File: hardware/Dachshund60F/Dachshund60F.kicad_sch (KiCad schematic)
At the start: 0 parts

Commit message: Add Dachshund60F schematic and PCB placement
- Schematic (one A2 sheet, 195 parts, ERC clean): MDBT50Q-1MV2 with
  32.768 kHz crystal, SWD and reset; MCP73831 charger (500 mA), JST-PH
  battery and power switch into VDDH; TPS22917-switched SK6812MINI-E
  LEDs; EC11 encoder; 6x15 COL2ROW matrix with 80 positions; JST-SH
  connector for a USB-C daughterboard. Module pins match board.json.
- PCB: all footprints placed from the KLE layout. Switches, stabilizers
  and encoder on the front, every SMD part on the back, and an 18 mm
  top strip for the module (antenna at the edge) and power parts.
  Not routed yet.
- Kailh MX hot-swap everywhere except SW604, SW606 and SW615, which use
  solder-only 3-pin footprints so the 6.25u and split spacebars can
  overlap.
- Vendor the keyswitch footprints (perigoso v2.4, CC-BY-SA-4.0) into
  hardware/Dachshund60F/lib, upgraded to the KiCad 10 format so Konnect
  can read them.
- .mcp.json: pin KiCad's IPC socket for Konnect.
- PROGRESS.md and the board README: design decisions and known DRC
  findings.

Co-Authored-By: Claude Opus 5.5 <noreply@anthropic.com>
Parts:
- added C1, C2, C3, C4, C6: 4.7uF, Capacitor_SMD:C_0603_1608Metric, symbol Device:C
- added C10, C11: 10nF, Capacitor_SMD:C_0402_1005Metric, symbol Device:C
- added C12: 1uF, Capacitor_SMD:C_0402_1005Metric, symbol Device:C
- added C13, C14, C5, C7: 100nF, Capacitor_SMD:C_0402_1005Metric, symbol Device:C
- added C8, C9: 12pF, Capacitor_SMD:C_0402_1005Metric, symbol Device:C
- added D1: BAT54WS, Diode_SMD:D_SOD-323, symbol Device:D_Schottky
- added D100, D101, D102, D103, D104, D105, D106, D107, D108, D109, D110, D111, D112, D113, D114, D200, D201, D202, D203, D204, D205, D206, D207, D208, D209, D210, D211, D212, D213, D300, D301, D302, D303, D304, D305, D306, D307, D308, D309, D310, D311, D312, D313, D400, D401, D402, D403, D404, D405, D406, D407, D408, D409, D410, D411, D413, D500, D501, D502, D503, D504, D505, D506, D507, D508, D509, D510, D512, D513, D600, D601, D603, D604, D606, D608, D610, D611, D612, D613, D614: 1N4148W, Diode_SMD:D_SOD-123, symbol Device:D
- added D2: SK6812MINI-E (Caps), LED_SMD:LED_SK6812MINI-E_3.2x2.8mm_P1.5mm_ReverseMount, symbol LED:SK6812MINI-E
- added D3: SK6812MINI-E (Layer), LED_SMD:LED_SK6812MINI-E_3.2x2.8mm_P1.5mm_ReverseMount, symbol LED:SK6812MINI-E
- added J1: USB daughterboard (JST-SH 4P), Connector_JST:JST_SH_SM04B-SRSS-TB_1x04-1MP_P1.00mm_Horizontal, symbol Connector_Generic_MountingPin:Conn_01x04_MountingPin
- added J2: Battery (JST-PH 2P), Connector_JST:JST_PH_S2B-PH-SM4-TB_1x02-1MP_P2.00mm_Horizontal, symbol Connector_Generic_MountingPin:Conn_01x02_MountingPin
- added J3: SWD, Connector_PinHeader_1.27mm:PinHeader_1x05_P1.27mm_Vertical, symbol Connector_Generic:Conn_01x05
- added R1: 2k, Resistor_SMD:R_0603_1608Metric, symbol Device:R
- added R2: 100k, Resistor_SMD:R_0402_1005Metric, symbol Device:R
- added ST1: Stab Backspace 2.00u, Keyswitch:Stabilizer_Cherry_MX_2.00u, symbol Mechanical:MountingHole
- added ST2: Stab Enter 2.25u, Keyswitch:Stabilizer_Cherry_MX_2.00u, symbol Mechanical:MountingHole
- added ST3: Stab Shift 2.25u, Keyswitch:Stabilizer_Cherry_MX_2.00u, symbol Mechanical:MountingHole
- added ST4: Stab Space 6.25u, Keyswitch:Stabilizer_Cherry_MX_6.25u, symbol Mechanical:MountingHole
- added ST5: Stab Space 2.75u, Keyswitch:Stabilizer_Cherry_MX_2.00u, symbol Mechanical:MountingHole
- added ST6: Stab Mod 2.25u, Keyswitch:Stabilizer_Cherry_MX_2.00u, symbol Mechanical:MountingHole
- added SW1: Power, Button_Switch_SMD:SW_SPDT_PCM12, symbol Switch:SW_SPDT
- added SW100: MX Esc (1.00u), Keyswitch:SW_Hotswap_Kailh_MX_1.00u, symbol Switch:SW_Push
- added SW101: MX F1 (1.00u), Keyswitch:SW_Hotswap_Kailh_MX_1.00u, symbol Switch:SW_Push
- added SW102: MX F2 (1.00u), Keyswitch:SW_Hotswap_Kailh_MX_1.00u, symbol Switch:SW_Push
- added SW103: MX F3 (1.00u), Keyswitch:SW_Hotswap_Kailh_MX_1.00u, symbol Switch:SW_Push
- added SW104: MX F4 (1.00u), Keyswitch:SW_Hotswap_Kailh_MX_1.00u, symbol Switch:SW_Push
- added SW105: MX F5 (1.00u), Keyswitch:SW_Hotswap_Kailh_MX_1.00u, symbol Switch:SW_Push
- added SW106: MX F6 (1.00u), Keyswitch:SW_Hotswap_Kailh_MX_1.00u, symbol Switch:SW_Push
- added SW107: MX F7 (1.00u), Keyswitch:SW_Hotswap_Kailh_MX_1.00u, symbol Switch:SW_Push
- added SW108: MX F8 (1.00u), Keyswitch:SW_Hotswap_Kailh_MX_1.00u, symbol Switch:SW_Push
- added SW109: MX F9 (1.00u), Keyswitch:SW_Hotswap_Kailh_MX_1.00u, symbol Switch:SW_Push
- added SW110: MX F10 (1.00u), Keyswitch:SW_Hotswap_Kailh_MX_1.00u, symbol Switch:SW_Push
- added SW111: MX F11 (1.00u), Keyswitch:SW_Hotswap_Kailh_MX_1.00u, symbol Switch:SW_Push
- added SW112: MX F12 (1.00u), Keyswitch:SW_Hotswap_Kailh_MX_1.00u, symbol Switch:SW_Push
- added SW113: MX Delete (1.00u), Keyswitch:SW_Hotswap_Kailh_MX_1.00u, symbol Switch:SW_Push
- added SW2: Reset, Button_Switch_SMD:SW_SPST_TL3342, symbol Switch:SW_Push
- added SW200: MX ` (1.00u), Keyswitch:SW_Hotswap_Kailh_MX_1.00u, symbol Switch:SW_Push
- added SW201: MX 1 (1.00u), Keyswitch:SW_Hotswap_Kailh_MX_1.00u, symbol Switch:SW_Push
- added SW202: MX 2 (1.00u), Keyswitch:SW_Hotswap_Kailh_MX_1.00u, symbol Switch:SW_Push
- added SW203: MX 3 (1.00u), Keyswitch:SW_Hotswap_Kailh_MX_1.00u, symbol Switch:SW_Push
- added SW204: MX 4 (1.00u), Keyswitch:SW_Hotswap_Kailh_MX_1.00u, symbol Switch:SW_Push
- added SW205: MX 5 (1.00u), Keyswitch:SW_Hotswap_Kailh_MX_1.00u, symbol Switch:SW_Push
- added SW206: MX 6 (1.00u), Keyswitch:SW_Hotswap_Kailh_MX_1.00u, symbol Switch:SW_Push
- added SW207: MX 7 (1.00u), Keyswitch:SW_Hotswap_Kailh_MX_1.00u, symbol Switch:SW_Push
- added SW208: MX 8 (1.00u), Keyswitch:SW_Hotswap_Kailh_MX_1.00u, symbol Switch:SW_Push
- added SW209: MX 9 (1.00u), Keyswitch:SW_Hotswap_Kailh_MX_1.00u, symbol Switch:SW_Push
- added SW210: MX 0 (1.00u), Keyswitch:SW_Hotswap_Kailh_MX_1.00u, symbol Switch:SW_Push
- added SW211: MX - (1.00u), Keyswitch:SW_Hotswap_Kailh_MX_1.00u, symbol Switch:SW_Push
- added SW212: MX = (1.00u), Keyswitch:SW_Hotswap_Kailh_MX_1.00u, symbol Switch:SW_Push
- added SW213: MX Backspace (2.00u), Keyswitch:SW_Hotswap_Kailh_MX_2.00u, symbol Switch:SW_Push
- added SW3: EC11E encoder, Rotary_Encoder:RotaryEncoder_Alps_EC11E-Switch_Vertical_H20mm, symbol Device:RotaryEncoder_Switch_MP
- added SW300: MX Tab (1.50u), Keyswitch:SW_Hotswap_Kailh_MX_1.50u, symbol Switch:SW_Push
- added SW301: MX Q (1.00u), Keyswitch:SW_Hotswap_Kailh_MX_1.00u, symbol Switch:SW_Push
- added SW302: MX W (1.00u), Keyswitch:SW_Hotswap_Kailh_MX_1.00u, symbol Switch:SW_Push
- added SW303: MX E (1.00u), Keyswitch:SW_Hotswap_Kailh_MX_1.00u, symbol Switch:SW_Push
- added SW304: MX R (1.00u), Keyswitch:SW_Hotswap_Kailh_MX_1.00u, symbol Switch:SW_Push
- added SW305: MX T (1.00u), Keyswitch:SW_Hotswap_Kailh_MX_1.00u, symbol Switch:SW_Push
- added SW306: MX Y (1.00u), Keyswitch:SW_Hotswap_Kailh_MX_1.00u, symbol Switch:SW_Push
- added SW307: MX U (1.00u), Keyswitch:SW_Hotswap_Kailh_MX_1.00u, symbol Switch:SW_Push
- added SW308: MX I (1.00u), Keyswitch:SW_Hotswap_Kailh_MX_1.00u, symbol Switch:SW_Push
- added SW309: MX O (1.00u), Keyswitch:SW_Hotswap_Kailh_MX_1.00u, symbol Switch:SW_Push
- added SW310: MX P (1.00u), Keyswitch:SW_Hotswap_Kailh_MX_1.00u, symbol Switch:SW_Push
- added SW311: MX [ (1.00u), Keyswitch:SW_Hotswap_Kailh_MX_1.00u, symbol Switch:SW_Push
- added SW312: MX ] (1.00u), Keyswitch:SW_Hotswap_Kailh_MX_1.00u, symbol Switch:SW_Push
- added SW313: MX \ (1.50u), Keyswitch:SW_Hotswap_Kailh_MX_1.50u, symbol Switch:SW_Push
- added SW400: MX Caps Lock (1.75u), Keyswitch:SW_Hotswap_Kailh_MX_1.75u, symbol Switch:SW_Push
- added SW401: MX A (1.00u), Keyswitch:SW_Hotswap_Kailh_MX_1.00u, symbol Switch:SW_Push
- added SW402: MX S (1.00u), Keyswitch:SW_Hotswap_Kailh_MX_1.00u, symbol Switch:SW_Push
- added SW403: MX D (1.00u), Keyswitch:SW_Hotswap_Kailh_MX_1.00u, symbol Switch:SW_Push
- added SW404: MX F (1.00u), Keyswitch:SW_Hotswap_Kailh_MX_1.00u, symbol Switch:SW_Push
- added SW405: MX G (1.00u), Keyswitch:SW_Hotswap_Kailh_MX_1.00u, symbol Switch:SW_Push
- added SW406: MX H (1.00u), Keyswitch:SW_Hotswap_Kailh_MX_1.00u, symbol Switch:SW_Push
- added SW407: MX J (1.00u), Keyswitch:SW_Hotswap_Kailh_MX_1.00u, symbol Switch:SW_Push
- added SW408: MX K (1.00u), Keyswitch:SW_Hotswap_Kailh_MX_1.00u, symbol Switch:SW_Push
- added SW409: MX L (1.00u), Keyswitch:SW_Hotswap_Kailh_MX_1.00u, symbol Switch:SW_Push
- added SW410: MX ; (1.00u), Keyswitch:SW_Hotswap_Kailh_MX_1.00u, symbol Switch:SW_Push
- added SW411: MX ' (1.00u), Keyswitch:SW_Hotswap_Kailh_MX_1.00u, symbol Switch:SW_Push
- added SW413: MX Enter (2.25u), Keyswitch:SW_Hotswap_Kailh_MX_2.25u, symbol Switch:SW_Push
- added SW500: MX Shift (2.25u), Keyswitch:SW_Hotswap_Kailh_MX_2.25u, symbol Switch:SW_Push
- added SW501: MX Z (1.00u), Keyswitch:SW_Hotswap_Kailh_MX_1.00u, symbol Switch:SW_Push
- added SW502: MX X (1.00u), Keyswitch:SW_Hotswap_Kailh_MX_1.00u, symbol Switch:SW_Push
- added SW503: MX C (1.00u), Keyswitch:SW_Hotswap_Kailh_MX_1.00u, symbol Switch:SW_Push
- added SW504: MX V (1.00u), Keyswitch:SW_Hotswap_Kailh_MX_1.00u, symbol Switch:SW_Push
- added SW505: MX B (1.00u), Keyswitch:SW_Hotswap_Kailh_MX_1.00u, symbol Switch:SW_Push
- added SW506: MX N (1.00u), Keyswitch:SW_Hotswap_Kailh_MX_1.00u, symbol Switch:SW_Push
- added SW507: MX M (1.00u), Keyswitch:SW_Hotswap_Kailh_MX_1.00u, symbol Switch:SW_Push
- added SW508: MX , (1.00u), Keyswitch:SW_Hotswap_Kailh_MX_1.00u, symbol Switch:SW_Push
- added SW509: MX . (1.00u), Keyswitch:SW_Hotswap_Kailh_MX_1.00u, symbol Switch:SW_Push
- added SW510: MX / (1.00u), Keyswitch:SW_Hotswap_Kailh_MX_1.00u, symbol Switch:SW_Push
- added SW512: MX Shift (1.75u), Keyswitch:SW_Hotswap_Kailh_MX_1.75u, symbol Switch:SW_Push
- added SW513: MX Up (1.00u), Keyswitch:SW_Hotswap_Kailh_MX_1.00u, symbol Switch:SW_Push
- added SW600, SW611: MX Ctrl (1.25u), Keyswitch:SW_Hotswap_Kailh_MX_1.25u, symbol Switch:SW_Push
- added SW601: MX Win (1.25u), Keyswitch:SW_Hotswap_Kailh_MX_1.25u, symbol Switch:SW_Push
- added SW603: MX Alt (1.25u), Keyswitch:SW_Hotswap_Kailh_MX_1.25u, symbol Switch:SW_Push
- added SW604: MX Mod (1.25u, solder), Button_Switch_Keyboard:SW_Cherry_MX_1.25u_Plate, symbol Switch:SW_Push
- added SW606: MX Space full (6.25u, solder), Button_Switch_Keyboard:SW_Cherry_MX_6.25u_Plate, symbol Switch:SW_Push
- added SW608: MX Mod (2.25u), Keyswitch:SW_Hotswap_Kailh_MX_2.25u, symbol Switch:SW_Push
- added SW610: MX Fn (1.25u), Keyswitch:SW_Hotswap_Kailh_MX_1.25u, symbol Switch:SW_Push
- added SW612: MX Left (1.00u), Keyswitch:SW_Hotswap_Kailh_MX_1.00u, symbol Switch:SW_Push
- added SW613: MX Down (1.00u), Keyswitch:SW_Hotswap_Kailh_MX_1.00u, symbol Switch:SW_Push
- added SW614: MX Right (1.00u), Keyswitch:SW_Hotswap_Kailh_MX_1.00u, symbol Switch:SW_Push
- added SW615: MX Space split (2.75u, solder), Button_Switch_Keyboard:SW_Cherry_MX_2.75u_Plate, symbol Switch:SW_Push
- added U1: MDBT50Q-1MV2, RF_Module:Raytac_MDBT50Q, symbol RF_Module:MDBT50Q-1MV2
- added U2: MCP73831-2-OT, Package_TO_SOT_SMD:SOT-23-5, symbol Battery_Management:MCP73831-2-OT
- added U3: TPS22917DBV, Package_TO_SOT_SMD:SOT-23-6, symbol Power_Management:TPS22917DBV
- added Y1: 32.768kHz 9pF, Crystal:Crystal_SMD_3215-2Pin_3.2x1.5mm, symbol Device:Crystal
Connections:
- new net: D406.2 (A), SW406.2
- new net: D313.2 (A), SW313.2
- new net: D110.2 (A), SW110.2
- new net: D200.2 (A), SW200.2
- new net: D210.2 (A), SW210.2
- new net: D100.2 (A), SW100.2
- new net: D300.2 (A), SW300.2
- new net: D213.2 (A), SW213.2
- new net: D613.2 (A), SW613.2
- new net: D600.2 (A), SW600.2
- new net: D308.2 (A), SW308.2
- new net: D305.2 (A), SW305.2
- new net: D403.2 (A), SW403.2
- new net: D604.2 (A), SW604.2
- new net: D608.2 (A), SW608.2
- new net: D601.2 (A), SW601.2
- new net: D301.2 (A), SW301.2
- new net: D107.2 (A), SW107.2
- new net: D507.2 (A), SW507.2
- new net: D205.2 (A), SW205.2
- new net: D407.2 (A), SW407.2
- new net: D102.2 (A), SW102.2
- new net: D405.2 (A), SW405.2
- new net: D307.2 (A), SW307.2
- new net: D108.2 (A), SW108.2
- new net: D400.2 (A), SW400.2
- new net: D501.2 (A), SW501.2
- new net: D109.2 (A), SW109.2
- new net: D510.2 (A), SW510.2
- new net: D303.2 (A), SW303.2
- new net: D402.2 (A), SW402.2
- new net: D312.2 (A), SW312.2
- new net: D310.2 (A), SW310.2
- new net: D508.2 (A), SW508.2
- new net: D409.2 (A), SW409.2
- new net: D413.2 (A), SW413.2
- new net: D201.2 (A), SW201.2
- new net: D207.2 (A), SW207.2
- new net: D208.2 (A), SW208.2
- new net: D306.2 (A), SW306.2
- new net: D502.2 (A), SW502.2
- new net: D112.2 (A), SW112.2
- new net: D105.2 (A), SW105.2
- new net: D408.2 (A), SW408.2
- new net: D610.2 (A), SW610.2
- new net: D509.2 (A), SW509.2
- new net: D113.2 (A), SW113.2
- new net: D203.2 (A), SW203.2
- new net: D410.2 (A), SW410.2
- new net: D106.2 (A), SW106.2
- new net: D612.2 (A), SW612.2
- new net: D302.2 (A), SW302.2
- new net: D211.2 (A), SW211.2
- new net: D202.2 (A), SW202.2
- new net: D614.2 (A), SW614.2
- new net: D603.2 (A), SW603.2
- new net: D503.2 (A), SW503.2
- new net: D404.2 (A), SW404.2
- new net: D611.2 (A), SW611.2
- new net: D111.2 (A), SW111.2
- new net: D204.2 (A), SW204.2
- new net: D504.2 (A), SW504.2
- new net: D103.2 (A), SW103.2
- new net: D209.2 (A), SW209.2
- new net: D512.2 (A), SW512.2
- new net: D304.2 (A), SW304.2
- new net: D500.2 (A), SW500.2
- new net: D311.2 (A), SW311.2
- new net: D101.2 (A), SW101.2
- new net: D411.2 (A), SW411.2
- new net: D212.2 (A), SW212.2
- new net: D401.2 (A), SW401.2
- new net: D309.2 (A), SW309.2
- new net: D506.2 (A), SW506.2
- new net: D505.2 (A), SW505.2
- new net: D206.2 (A), SW206.2
- new net: D513.2 (A), SW513.2
- new net: D104.2 (A), SW104.2
- new net +3V3: C6.1, C7.1, J3.1 (Pin_1), U1.28 (VDD)
- new net CHG_STAT: D1.2 (A), U1.39 (P0.15)
- new net COL0: SW100.1, SW200.1, SW300.1, SW400.1, SW500.1, SW600.1, U1.11 (P0.02)
- new net COL1: SW101.1, SW201.1, SW301.1, SW401.1, SW501.1, SW601.1, U1.9 (P0.03)
- new net COL10: SW110.1, SW210.1, SW310.1, SW410.1, SW510.1, SW610.1, U1.59 (P1.05)
- new net COL11: SW111.1, SW211.1, SW311.1, SW411.1, SW611.1, U1.57 (P1.06)
- new net COL12: SW112.1, SW212.1, SW312.1, SW512.1, SW612.1, U1.58 (P1.07)
- new net COL13: SW113.1, SW213.1, SW313.1, SW413.1, SW513.1, SW613.1, U1.20 (P0.04)
- new net COL14: SW3.S1, SW614.1, U1.21 (P0.05)
- new net COL2: SW102.1, SW202.1, SW302.1, SW402.1, SW502.1, U1.13 (P0.28)
- new net COL3: SW103.1, SW203.1, SW303.1, SW403.1, SW503.1, SW603.1, U1.10 (P0.29)
- new net COL4: SW104.1, SW204.1, SW304.1, SW404.1, SW504.1, SW604.1, U1.14 (P0.30)
- new net COL5: SW105.1, SW205.1, SW305.1, SW405.1, SW505.1, U1.12 (P0.31)
- new net COL6: SW106.1, SW206.1, SW306.1, SW406.1, SW506.1, SW606.1, SW615.1, U1.61 (P1.01)
- new net COL7: SW107.1, SW207.1, SW307.1, SW407.1, SW507.1, U1.50 (P1.02)
- new net COL8: SW108.1, SW208.1, SW308.1, SW408.1, SW508.1, SW608.1, U1.60 (P1.03)
- new net COL9: SW109.1, SW209.1, SW309.1, SW409.1, SW509.1, U1.56 (P1.04)
- new net ENC_A: C10.1, SW3.A, U1.27 (P0.11)
- new net ENC_B: C11.1, SW3.B, U1.29 (P0.12)
- new net ENC_SW: D114.2 (A), SW3.S2
- new net GND: C1.2, C10.2, C11.2, C12.2, C13.2, C14.2, C2.2, C3.2, C4.2, C5.2, C6.2, C7.2, C8.2, C9.2, D2.1 (VSS), D3.1 (VSS), J1.4 (Pin_4), J1.MP (MountPin), J2.2 (Pin_2), J3.5 (Pin_5), R1.2, R2.2, SW2.2, SW3.C, SW3.MP, U1.1 (GND), U1.15 (GND), U1.2 (GND), U1.33 (GND), U1.55 (GND), U2.2 (V_{SS}), U3.2 (GND)
- new net LED_D1: D2.4 (DOUT), D3.2 (DIN)
- new net LED_DIN: D2.2 (DIN), U1.22 (P0.06)
- new net LED_EN: R2.1, U1.24 (P0.08), U3.3 (ON)
- new net LED_VDD: C13.1, C14.1, D2.3 (VDD), D3.3 (VDD), U3.6 (VOUT)
- new net NRESET: J3.4 (Pin_4), SW2.1, U1.40 (P0.18)
- new net PROG: R1.1, U2.5 (PROG)
- new net ROW0: D100.1 (K), D101.1 (K), D102.1 (K), D103.1 (K), D104.1 (K), D105.1 (K), D106.1 (K), D107.1 (K), D108.1 (K), D109.1 (K), D110.1 (K), D111.1 (K), D112.1 (K), D113.1 (K), D114.1 (K), U1.3 (P1.10)
- new net ROW1: D200.1 (K), D201.1 (K), D202.1 (K), D203.1 (K), D204.1 (K), D205.1 (K), D206.1 (K), D207.1 (K), D208.1 (K), D209.1 (K), D210.1 (K), D211.1 (K), D212.1 (K), D213.1 (K), U1.4 (P1.11)
- new net ROW2: D300.1 (K), D301.1 (K), D302.1 (K), D303.1 (K), D304.1 (K), D305.1 (K), D306.1 (K), D307.1 (K), D308.1 (K), D309.1 (K), D310.1 (K), D311.1 (K), D312.1 (K), D313.1 (K), U1.5 (P1.12)
- new net ROW3: D400.1 (K), D401.1 (K), D402.1 (K), D403.1 (K), D404.1 (K), D405.1 (K), D406.1 (K), D407.1 (K), D408.1 (K), D409.1 (K), D410.1 (K), D411.1 (K), D413.1 (K), U1.6 (P1.13)
- new net ROW4: D500.1 (K), D501.1 (K), D502.1 (K), D503.1 (K), D504.1 (K), D505.1 (K), D506.1 (K), D507.1 (K), D508.1 (K), D509.1 (K), D510.1 (K), D512.1 (K), D513.1 (K), U1.7 (P1.14)
- new net ROW5: D600.1 (K), D601.1 (K), D603.1 (K), D604.1 (K), D606.1 (K), D608.1 (K), D610.1 (K), D611.1 (K), D612.1 (K), D613.1 (K), D614.1 (K), U1.8 (P1.15)
- new net SPACE_SW: D606.2 (A), SW606.2, SW615.2
- new net STAT_RAW: D1.1 (K), U2.1 (STAT)
- new net SWDCLK: J3.3 (Pin_3), U1.53 (SWDCLK)
- new net SWDIO: J3.2 (Pin_2), U1.51 (SWDIO)
- new net USB_DM: J1.2 (Pin_2), U1.34 (D-)
- new net USB_DP: J1.3 (Pin_3), U1.35 (D+)
- new net VBAT: C3.1, J2.1 (Pin_1), SW1.1 (A), U2.3 (V_{BAT})
- new net VBUS: C1.1, C2.1, J1.1 (Pin_1), U1.32 (VBUS), U2.4 (V_{DD})
- new net VSYS: C12.1, C4.1, C5.1, SW1.2 (B), U1.30 (VDDH), U3.1 (VIN)
- new net XL1: C8.1, U1.17 (P0.00), Y1.1
- new net XL2: C9.1, U1.18 (P0.01), Y1.2
- no-connect marks 0 -> 25

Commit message: Route Dachshund60F PCB with horizontal encoder and compact layout
- Encoder: replace the vertical EC11 with a Bourns PEC12R-4220F-S0024
  horizontal encoder (24 detents, push) so a wide roller turns like a
  mouse wheel. The body sits just past 16u; the board is about 12.7 mm
  wider.
- Layout: drop the 18 mm top strip. The module (antenna at the right
  edge), charger, connectors, power switch, reset, SWD and LED load
  switch move to the empty column under the encoder. Outline is now
  318.5 x 121.1 mm.
- Routing: Freerouting 2.5.0 autorouted all signal and power nets
  (0.25 mm signal, 0.3 mm power), with an antenna keep-out added to the
  DSN. GND pours on both layers, stitching vias, and solid pour
  connections to SMD pads.
- DRC: min track width 0.15 mm; Dachshund60F.kicad_dru allows 0.2 mm at
  the LED cutouts and 0 mm for the edge-mount power switch tabs.
- Open: C5, C6 and C7 GND pads beside the module are still unconnected
  and need a hand reroute (see PROGRESS.md).

Co-Authored-By: Claude Opus 5.5 <noreply@anthropic.com>
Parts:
- SW3: value EC11E encoder -> PEC12R-4220F-S0024 (horizontal, 20 mm shaft); footprint Rotary_Encoder:RotaryEncoder_Alps_EC11E-Switch_Vertical_H20mm -> Rotary_Encoder:RotaryEncoder_Bourns_Horizontal_PEC12R-2x17F-Sxxxx; symbol Device:RotaryEncoder_Switch_MP -> Device:RotaryEncoder_Switch
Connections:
- net GND: no longer SW3.MP
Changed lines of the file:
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@@
 	(wire
 		(pts
-			(xy 30.48 337.82)
-			(xy 30.48 340.36)
-		)
-	)
-	(wire
-		(pts
 			(xy 53.34 349.25)
 			(xy 53.34 351.79)
@@
 	)
 	(label "GND"
-		(at 30.48 340.36 0)
-		(effects
-			(font
-				(size 1.27 1.27)
-			)
-			(justify left bottom)
-		)
-	)
-	(label "GND"
 		(at 53.34 351.79 0)
 		(effects
@@
 	)
 	(symbol
-		(lib_id "Device:RotaryEncoder_Switch_MP")
+		(lib_id "Device:RotaryEncoder_Switch")
 		(at 30.48 330.2 0)
 		(unit 1)
@@
 			)
 		)
-		(property "Value" "EC11E encoder"
+		(property "Value" "PEC12R-4220F-S0024 (horizontal, 20 mm shaft)"
 			(at 30.48 323.85 0)
 			(effects
@@
 			)
 		)
-		(property "Footprint" "Rotary_Encoder:RotaryEncoder_Alps_EC11E-Switch_Vertical_H20mm"
+		(property "Footprint" "Rotary_Encoder:RotaryEncoder_Bourns_Horizontal_PEC12R-2x17F-Sxxxx"
 			(at 30.48 330.2 0)
 			(hide yes)
@@
 			)
 		)
-		(property "Datasheet" ""
+		(property "Datasheet" "https://www.bourns.com/docs/product-datasheets/pec12r.pdf"
 			(at 30.48 330.2 0)
 			(hide yes)

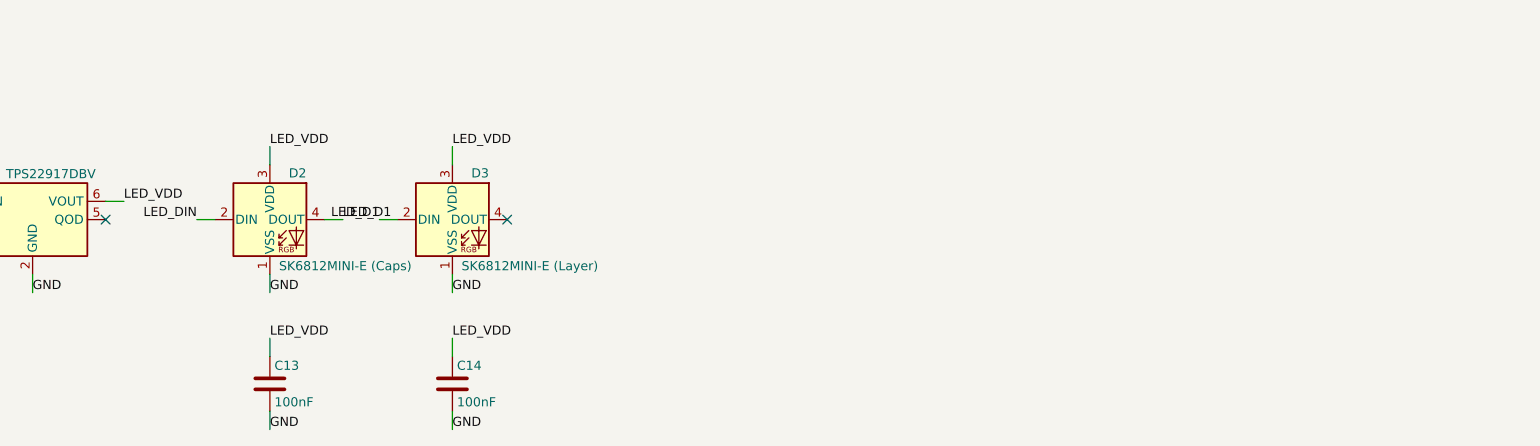
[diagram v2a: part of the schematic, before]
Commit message: Add layer and battery indicator row; round board corners
Move the layer LED from under Esc to a row of five reverse-mount
SK6812MINI-E LEDs above the Right arrow: layer, then a 4-step battery
gauge (D4-D7, each with a 100 nF cap). The chain is now U1 P0.06 ->
D3 (layer) -> D4..D7 (battery) -> D2 (Caps Lock).

- Re-route the whole board. The router now keeps clear of the LED
  cutouts and of a 0.35 mm band along the board edge, including the
  corners. DRC: 0 errors and 0 unconnected items, besides the 7 excluded
  spacebar items.
- Board corner radius is 5 mm (was 1 mm).
- Extend the 0.2 mm LED cutout edge rule to D2-D7.
- board.json: 6 indicators. keyboard.json: indicator id is the chain
  index; free-standing LEDs use an `at` position and battery LEDs a
  `level`. New host-lib tests check chain ids, positions, and that no
  free-standing LED sits under a key.

Co-Authored-By: Claude Opus 5.5 <noreply@anthropic.com>
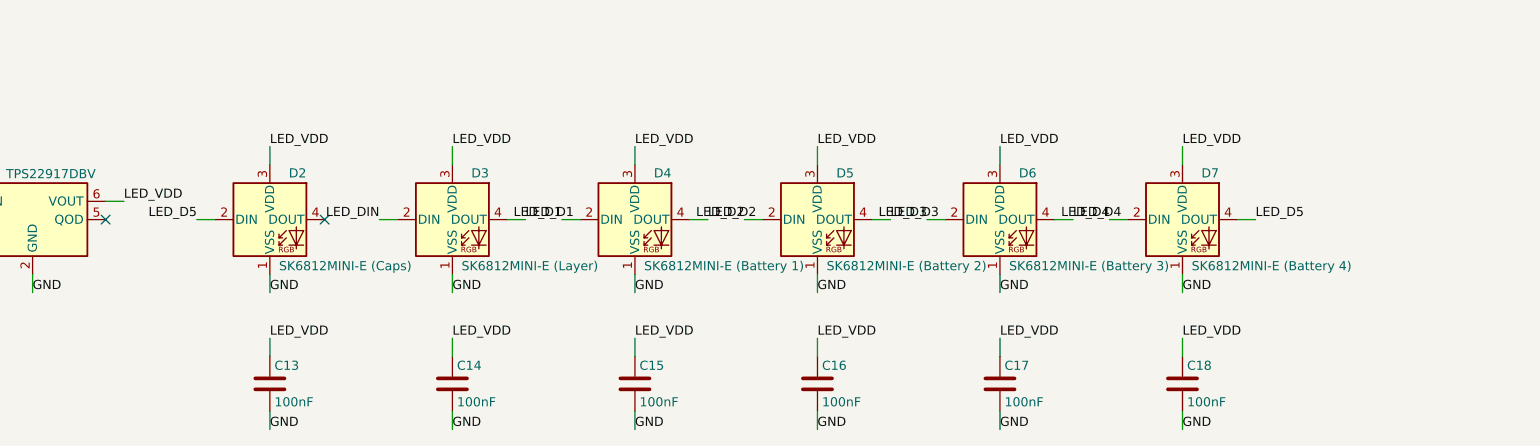
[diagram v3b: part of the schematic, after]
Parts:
- added C15, C16, C17, C18: 100nF, Capacitor_SMD:C_0402_1005Metric, symbol Device:C
- added D4: SK6812MINI-E (Battery 1), LED_SMD:LED_SK6812MINI-E_3.2x2.8mm_P1.5mm_ReverseMount, symbol LED:SK6812MINI-E
- added D5: SK6812MINI-E (Battery 2), LED_SMD:LED_SK6812MINI-E_3.2x2.8mm_P1.5mm_ReverseMount, symbol LED:SK6812MINI-E
- added D6: SK6812MINI-E (Battery 3), LED_SMD:LED_SK6812MINI-E_3.2x2.8mm_P1.5mm_ReverseMount, symbol LED:SK6812MINI-E
- added D7: SK6812MINI-E (Battery 4), LED_SMD:LED_SK6812MINI-E_3.2x2.8mm_P1.5mm_ReverseMount, symbol LED:SK6812MINI-E
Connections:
- net GND: now also C15.2, C16.2, C17.2, C18.2, D4.1 (VSS), D5.1 (VSS), D6.1 (VSS), D7.1 (VSS)
- net LED_D1: now also D3.4 (DOUT), D4.2 (DIN); no longer D2.4 (DOUT), D3.2 (DIN)
- net LED_DIN: now also D3.2 (DIN); no longer D2.2 (DIN)
- net LED_VDD: now also C15.1, C16.1, C17.1, C18.1, D4.3 (VDD), D5.3 (VDD), D6.3 (VDD), D7.3 (VDD)
- new net LED_D2: D4.4 (DOUT), D5.2 (DIN)
- new net LED_D3: D5.4 (DOUT), D6.2 (DIN)
- new net LED_D4: D6.4 (DOUT), D7.2 (DIN)
- new net LED_D5: D2.2 (DIN), D7.4 (DOUT)
